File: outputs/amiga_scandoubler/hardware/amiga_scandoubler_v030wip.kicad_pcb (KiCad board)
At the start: 4 copper layers, 95 x 95 mm, 139 parts, among them J1 HYC06-HDR15B-060, J2 HYC06-HDR15B-060, J3 TYPE-C-31-M-12, J4 JTAG 2x05 2.54mm, U1 TVP7002PZP, U2 GW1N-LV4QN88C6/I5, U3 ADV7125KSTZ140, U4 SN74LVC2G17DBVR, U5 SN74LVC2G17DBVR, U6 SN74LVC1G17DBVR, U7 TPS62160DSGR, U8 TPS62160DSGR, U9 TPS62160DSGR, Y1 27MHz OT2EL4C4JI-111OLP-27M

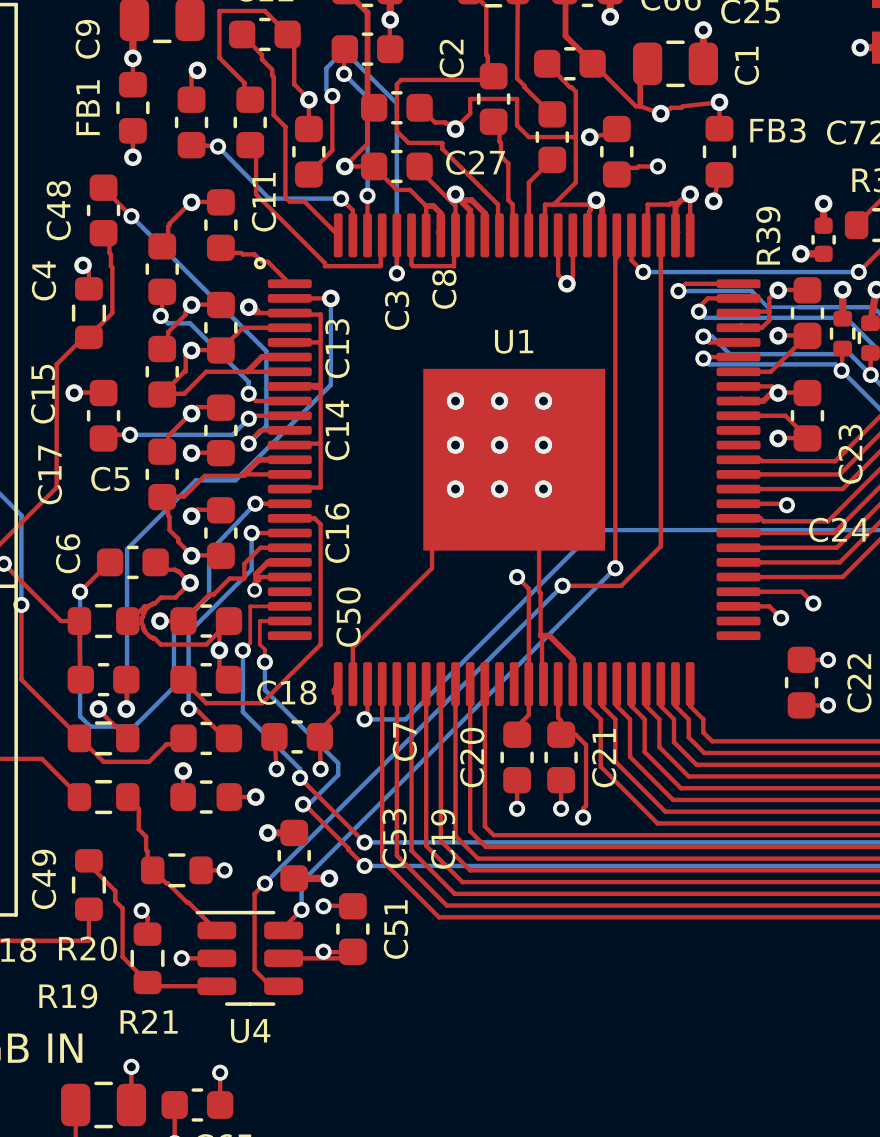
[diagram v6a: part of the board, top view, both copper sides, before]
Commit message: Tidy GND between C27 and U1.90-92, spread C21's vias, merge U4.5-C51 parallel lines
- dfm_tidy2.py: U1.91 straight into the GND via, U1.90 joins U1.91's corner, C27.2 into the via centre;
  C21 3V3 via moved 0.26 -> 0.47 mm from its GND via; U4.5 -> via -> C51 as one line
- no overlapping vias board-wide; no same-net parallel lines with a gap < 0.15 mm left
- DRC 0/0, audit PASS, 570-node netlist match, no pad lost/narrowed its connection; fab outputs regenerated

Co-Authored-By: Claude Opus 5.5 <noreply@anthropic.com>
Claude-Session: https://claude.ai/code/session_019f929sAJ7LRnJRRFvA6g9F
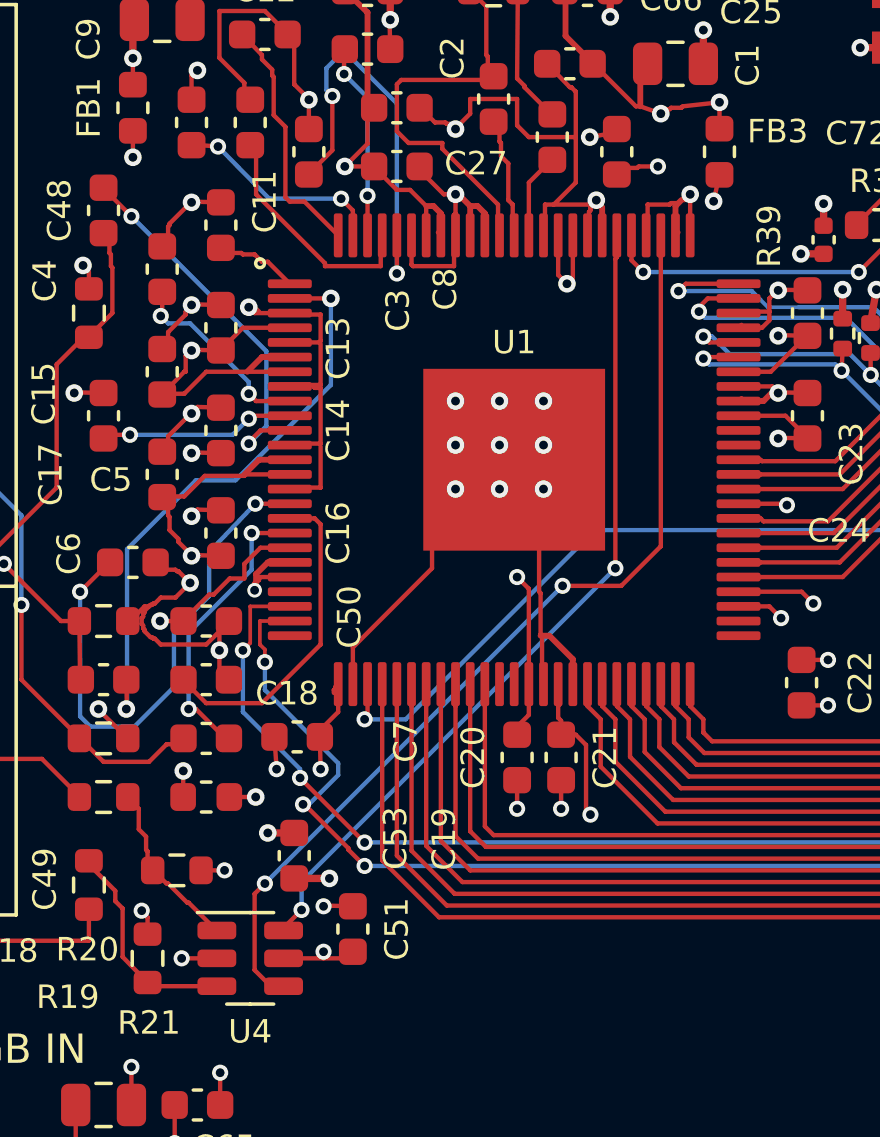
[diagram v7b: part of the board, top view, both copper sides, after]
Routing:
- net 3V3: track 82.6 -> 81.4 mm

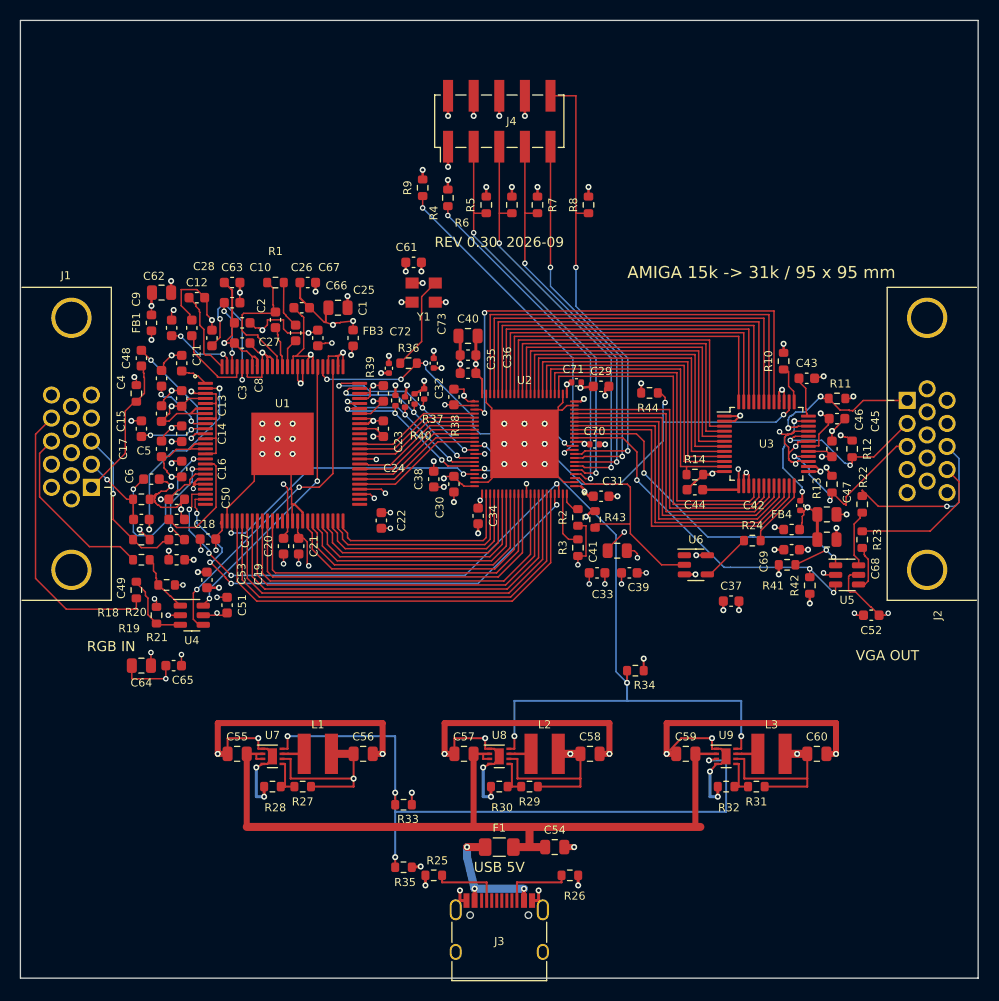
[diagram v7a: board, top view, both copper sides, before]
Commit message: Smooth the router's 0.05-grid staircases into long straight / 45-degree runs
- dfm_planeloop.py: GND/3V3 detours (thin, jogged) that only duplicate the plane removed (R16-C18 arc, U3 GND stub)
- dfm_smooth.py (+ tools/trackchains.py): chains redrawn by greedy pull-taut with 1-2 octilinear segments,
  clearance 0.2 to other nets, no same-net pads/vias other than the chain's ends; 2 passes, 399 -> 191 segments
- dfm_tidy3.py: hand fixes where T-junctions pin the chain (U1.77/79 GND, U1.13/14, FB4-C42-C47, U2 corner GND)
- tools/jogscan.py: short jogs 198 -> 14 (corner chamfers etc. left); pcbedit.remove_segment(dup_ok)
- DRC 0/0, audit PASS, 570-node netlist match, no pad lost/narrowed its connection, no overlaps,
  no tracks in pin gaps; fab outputs regenerated (BOM/CPL unchanged)

Co-Authored-By: Claude Opus 5.5 <noreply@anthropic.com>
Claude-Session: https://claude.ai/code/session_019f929sAJ7LRnJRRFvA6g9F
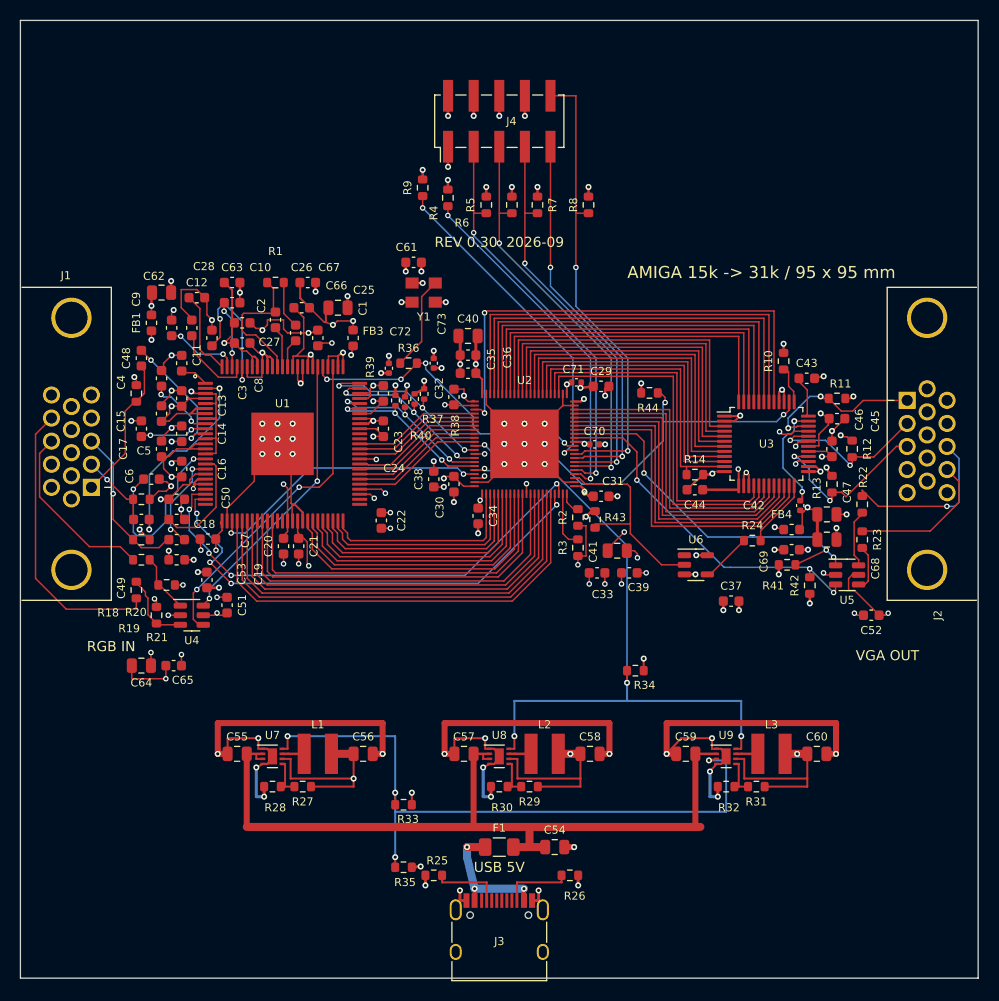
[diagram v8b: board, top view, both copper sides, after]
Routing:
- net GND: track 342.3 -> 330.8 mm
- net 1V2: track 112.8 -> 111.1 mm
- net DAC_3V3: track 46.8 -> 45.6 mm
- net B_OUT: track 19.2 -> 18.0 mm
- net ADC_1V9A: track 60.9 -> 59.9 mm
